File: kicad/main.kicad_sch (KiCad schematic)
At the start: 64 parts, among them J1 Jack-DC, J12 I2C1, J14 LCD_Conn, J15 VIA_A, J2 UART, J3 Data, J4 PWR, J5 uSD, J7 IO~{EN}_{[3..4]}, J8 Control, J9 Addr, P1 Mini-DIN-6, SW2 Reset, SW3 SW_PWR, U1 GAL20V8, U2 74HC00, U3 AMS1117, U4 DS1307N+, U5 MCP9808_MSOP, U7 ESP-01, X1 16 MHz, X2 1.8432 MHz, Y1 32.768 KHz

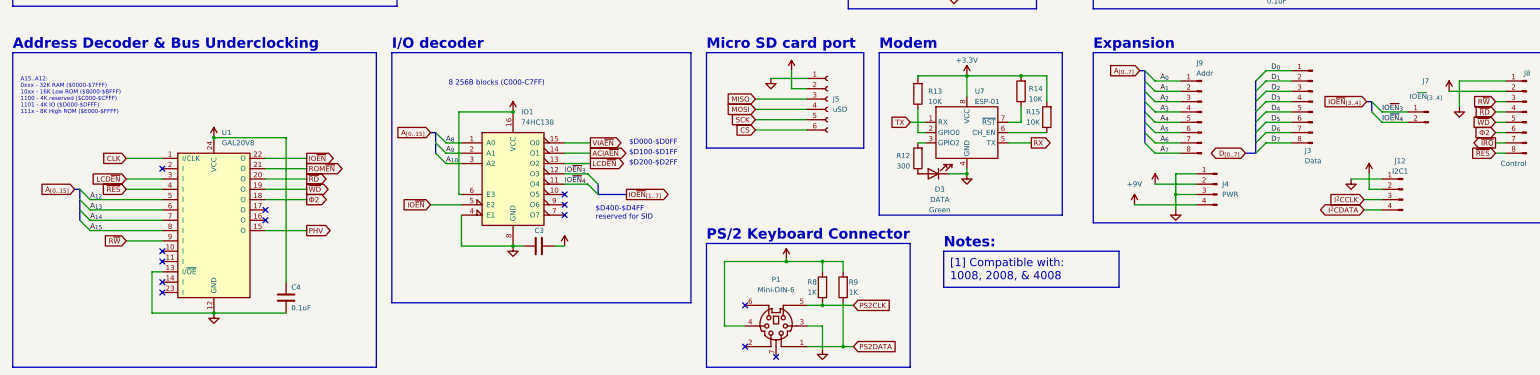
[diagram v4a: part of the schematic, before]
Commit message: Replace GAL20V8 with GAL(ATF)16V8
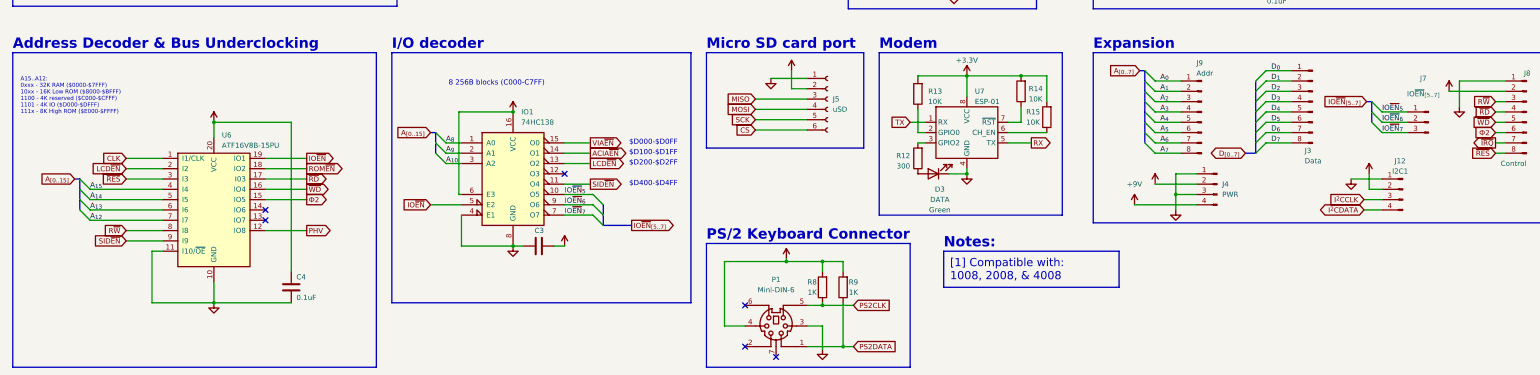
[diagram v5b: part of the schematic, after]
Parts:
- removed J7: IO~{EN}_{[3..4]}, Connector_PinHeader_2.54mm:PinHeader_1x02_P2.54mm_Vertical, symbol Connector:Conn_01x02_Pin
- removed U1: GAL20V8, Package_DIP:DIP-24_W7.62mm_Socket, symbol my:GAL20V8
- added J7: IO~{EN}_{[5..7]}, Connector_PinHeader_2.54mm:PinHeader_1x03_P2.54mm_Vertical, symbol Connector:Conn_01x03_Pin
- added U6: ATF16V8B-15PU, Package_DIP:DIP-20_W7.62mm_Socket, symbol Logic_Programmable:GAL16V8
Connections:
- net +5V: now also U6.20 (VCC)
- net A_{12}: now also U6.7 (I7)
- net A_{13}: now also U6.6 (I6)
- net A_{14}: now also U6.5 (I5)
- net A_{15}: now also U6.4 (I4)
- net CLK: now also U6.1 (I1/CLK)
- net GND: now also U6.10 (GND), U6.11 (I10/~{OE})
- net IO~{EN}: now also U6.19 (IO1)
- net LCD~{EN}: now also U6.2 (I2)
- net PHV: now also U6.12 (IO8)
- net ROM~{EN}: now also U6.18 (IO2)
- net R~{W}: now also U6.8 (I8)
- net ~{RD}: now also U6.17 (I03)
- net ~{RES}: now also U6.3 (I3)
- net ~{WD}: now also U6.16 (IO4)
- net Ф2: now also U6.15 (IO5)
- net IO~{EN}_{5}: now reaches IO1.10 (O5)
- net IO~{EN}_{5}: now also J7.1 (Pin_1)
- net IO~{EN}_{7}: now reaches IO1.7 (O7)
- net IO~{EN}_{7}: now also J7.3 (Pin_3)
- net IO~{EN}_{6}: now reaches IO1.9 (O6)
- net IO~{EN}_{6}: now also J7.2 (Pin_2)
- net IO~{EN}_{3}: no longer names the net of IO1.12 (O3)
- net IO~{EN}_{4} renamed SID~{EN}
- net SID~{EN}: now also U6.9 (I9)
- no-connect marks 32 -> 25
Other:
- note added: "$D400-$D4FF"
- note removed: "$D400-$D4FF reserved for SID"
- moved on the sheet: C4

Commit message: Generate top silk layer with Kicad
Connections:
- net +9V renamed +5VA
- net RX renamed ACIARX
- net TX renamed ACIATX
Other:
- moved on the sheet: C1, C10, C12, C3, C4, D1, D2, D3, IO1, J5, MH1, MH2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

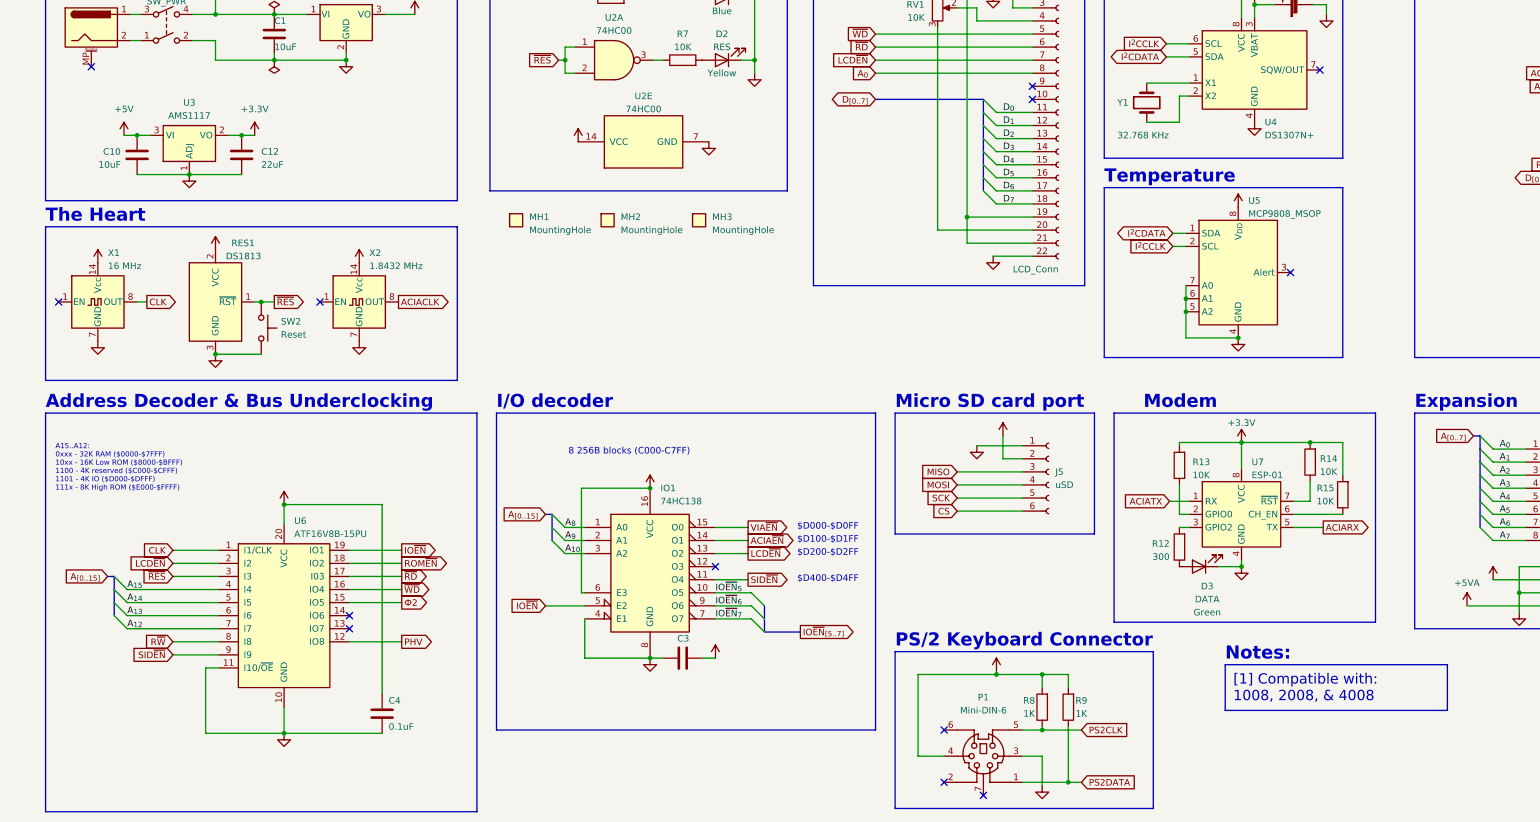
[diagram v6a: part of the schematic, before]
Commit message: Route /RST to ESP-01
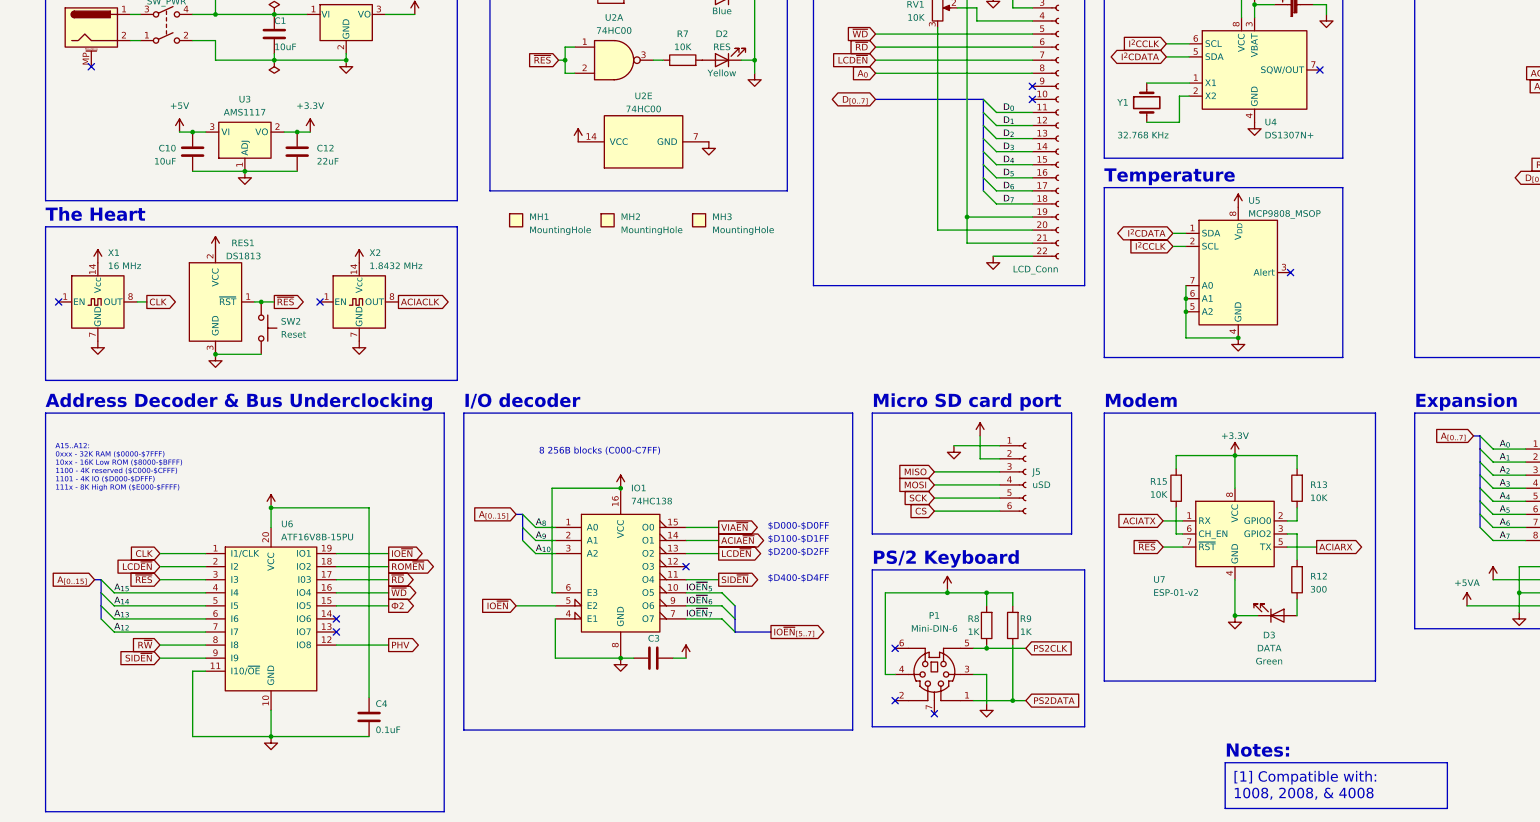
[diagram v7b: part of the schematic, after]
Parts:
- removed R14: 10K, Resistor_THT:R_Axial_DIN0204_L3.6mm_D1.6mm_P7.62mm_Horizontal, symbol Device:R
- removed U7: ESP-01, my:ESP-01, symbol my:ESP-01
- added U7: ESP-01-v2, my:ESP-01, symbol my:ESP-01-v2
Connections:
- net +3.3V: now also U7.8 (VCC)
- net ACIARX: now also U7.5 (TX)
- net ACIATX: now also U7.1 (RX)
- net GND: now also U7.4 (GND)
- net ~{RES}: now also U7.7 (~{RST})
- net at R13.1: now also U7.2 (GPIO0)
- net at R12.2: now also U7.3 (GPIO2)
- net at R15.1: now also U7.6 (CH_EN)
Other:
- note added: "PS/2 Keyboard"
- note removed: "PS/2 Keyboard Connector"
- moved on the sheet: C10, C12, C3, C4, IO1, J5, P1, R8, R9, U3, U6

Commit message: Rename project to Deck65
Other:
- title: 65ad02 -> deck65
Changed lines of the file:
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@@
   (paper "A3")
   (title_block
-    (title "65ad02")
+    (title "deck65")
     (date "2023-05-10")
     (rev "16")
